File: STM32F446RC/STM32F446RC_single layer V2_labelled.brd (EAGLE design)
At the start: 74.9 x 25.4 mm, 75 parts, among them IC1 STM32F446RCT6

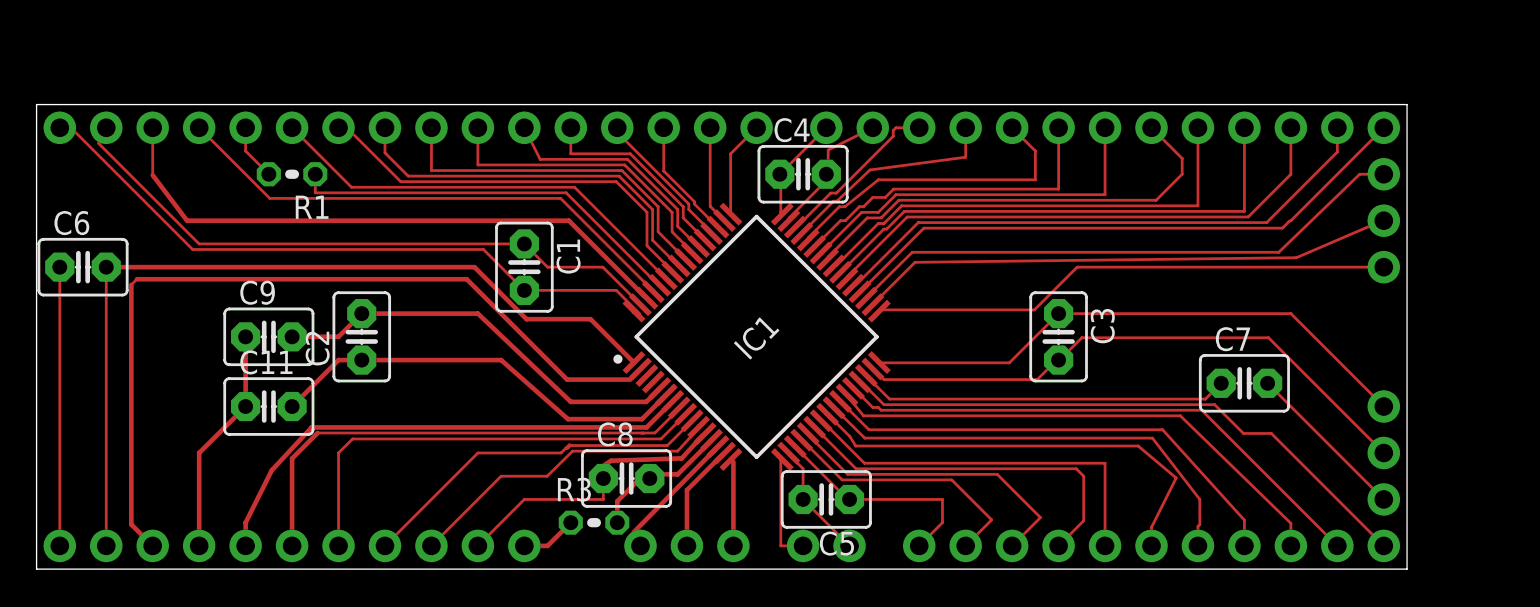
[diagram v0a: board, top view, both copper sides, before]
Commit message: added double layer
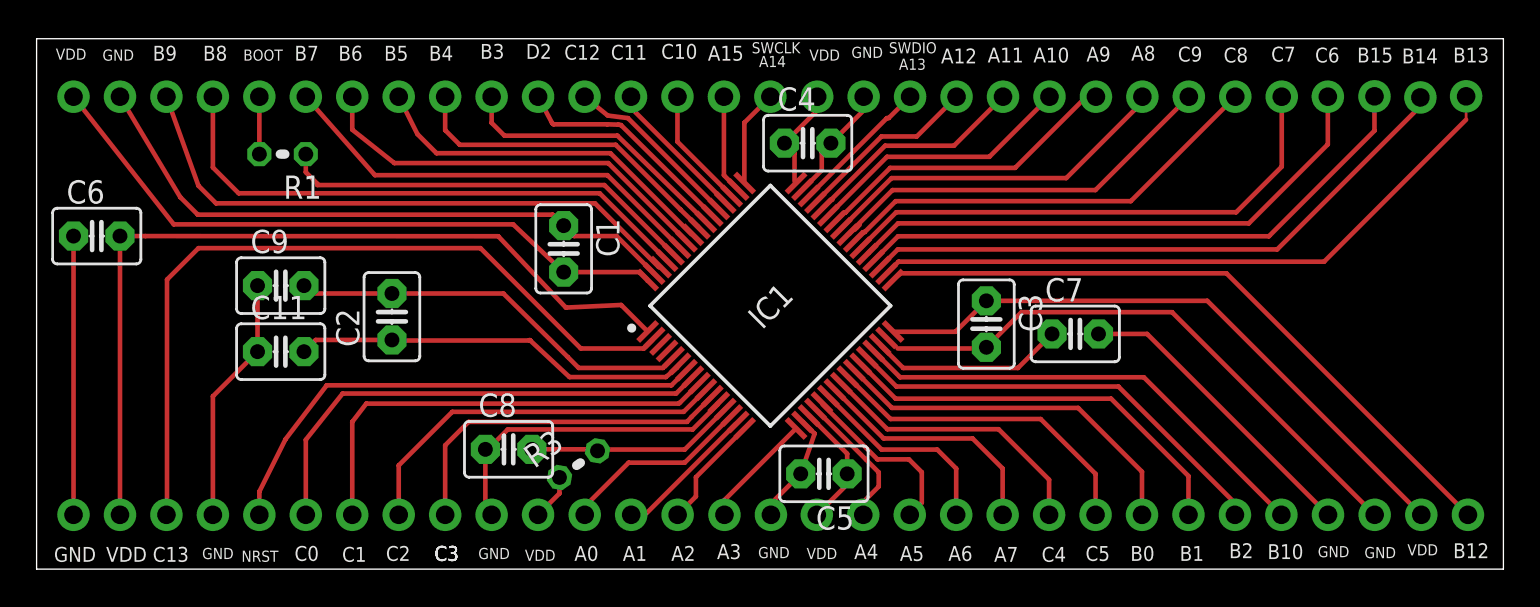
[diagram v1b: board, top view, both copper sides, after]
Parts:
- C1, C3, C4, C5, C6: value 100n+1u -> 100n
- C11, C2, C9: value 20p -> 22p
- R3: value (none) -> 47
- moved JP18 14.3 mm to (78.3, 2.97)
- moved C7 9.64 mm to (56.8, 12.9)
- moved JP13 8.15 mm to (78.2, 25.9)
- moved C8 6.64 mm to (25.8, 6.55)
- moved JP51 6.26 mm to (75.7, 2.97)
- moved JP16 5.85 mm to (65.5, 2.97)
- moved JP22 5.85 mm to (60.4, 2.97)
- moved JP11 5.85 mm to (52.8, 2.97)
- moved JP12 5.85 mm to (55.4, 2.97)
- moved JP17 5.85 mm to (63.0, 2.97)
- moved JP19 5.85 mm to (47.7, 2.97)
- moved JP23 5.85 mm to (57.9, 2.97)
- moved JP48 5.85 mm to (42.7, 2.97)
- moved JP9 5.85 mm to (50.3, 2.97)
- moved JP14 5.85 mm to (68.1, 2.97)
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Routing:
- net N$66: track 20.3 -> 10.7 mm
- net N$11: track 24.5 -> 15.5 mm
- net N$18: track 20.2 -> 11.2 mm
- net N$21: track 28.6 -> 37.0 mm
- net N$54: track 9.09 -> 16.8 mm
- net N$17: track 21.0 -> 13.6 mm
- net N$22: track 29.3 -> 36.7 mm
- net N$19: track 16.8 -> 9.67 mm
- net N$12: track 24.9 -> 18.0 mm
- net N$52: track 14.2 -> 7.65 mm
- net N$16: track 32.3 -> 26.1 mm
- net N$13: track 26.3 -> 20.4 mm
- net N$14: track 28.4 -> 22.7 mm
- net N$15: track 30.0 -> 24.2 mm
- net N$64: track 12.3 -> 7.41 mm
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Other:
- board size 74.9 x 25.4 mm -> 80.2 x 29 mm
- board text added: "A0"
- board text added: "A1"
- board text added: "A10"
- board text added: "A11"
- board text added: "A12"
- board text added: "A13"
- board text added: "A14"
- board text added: "A15"
- board text added: "A2"
- board text added: "A3"
- board text added: "A4"
- board text added: "A5"
- board text added: "A6"
- board text added: "A7"
- board text added: "A8"
- board text added: "A9"
- board text added: "B0"
- board text added: "B1"
- board text added: "B10"
- board text added: "B12"
- board text added: "B13"
- board text added: "B14"
- board text added: "B15"
- board text added: "B2"
- board text added: "B3"
- board text added: "B4"
- board text added: "B5"
- board text added: "B6"
- board text added: "B7"
- board text added: "B8"
- board text added: "B9"
- board text added: "BOOT"
- board text added: "C0"
- board text added: "C1"
- board text added: "C10"
- board text added: "C11"
- board text added: "C12"
- board text added: "C13"
- board text added: "C2"
- board text added: "C3"
- board text added: "C4"
- board text added: "C5"
- board text added: "C6"
- board text added: "C7"
- board text added: "C8"
- board text added: "C9"
- board text added: "D2"
- board text added: "GND"
- board text added: "NRST"
- board text added: "SWCLK"
- board text added: "SWDIO"
- board text added: "VDD"

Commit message: added final
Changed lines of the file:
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@@
 <layer number="16" name="Bottom" color="1" fill="1" visible="yes" active="yes"/>
 <layer number="17" name="Pads" color="2" fill="1" visible="yes" active="yes"/>
-<layer number="18" name="Vias" color="2" fill="1" visible="no" active="yes"/>
+<layer number="18" name="Vias" color="2" fill="1" visible="yes" active="yes"/>
 <layer number="19" name="Unrouted" color="6" fill="1" visible="yes" active="yes"/>
 <layer number="20" name="Dimension" color="24" fill="1" visible="yes" active="yes"/>
 <layer number="21" name="tPlace" color="7" fill="1" visible="yes" active="yes"/>
-<layer number="22" name="bPlace" color="7" fill="1" visible="no" active="yes"/>
+<layer number="22" name="bPlace" color="7" fill="1" visible="yes" active="yes"/>
 <layer number="23" name="tOrigins" color="15" fill="1" visible="yes" active="yes"/>
-<layer number="24" name="bOrigins" color="15" fill="1" visible="no" active="yes"/>
-<layer number="25" name="tNames" color="7" fill="1" visible="no" active="yes"/>
-<layer number="26" name="bNames" color="7" fill="1" visible="no" active="yes"/>
-<layer number="27" name="tValues" color="7" fill="1" visible="no" active="yes"/>
-<layer number="28" name="bValues" color="7" fill="1" visible="no" active="yes"/>
-<layer number="29" name="tStop" color="7" fill="3" visible="no" active="yes"/>
+<layer number="24" name="bOrigins" color="15" fill="1" visible="yes" active="yes"/>
+<layer number="25" name="tNames" color="7" fill="1" visible="yes" active="yes"/>
+<layer number="26" name="bNames" color="7" fill="1" visible="yes" active="yes"/>
+<layer number="27" name="tValues" color="7" fill="1" visible="yes" active="yes"/>
+<layer number="28" name="bValues" color="7" fill="1" visible="yes" active="yes"/>
+<layer number="29" name="tStop" color="7" fill="3" visible="yes" active="yes"/>
 <layer number="30" name="bStop" color="7" fill="6" visible="no" active="yes"/>
-<layer number="31" name="tCream" color="7" fill="4" visible="no" active="yes"/>
-<layer number="32" name="bCream" color="7" fill="5" visible="no" active="yes"/>
-<layer number="33" name="tFinish" color="6" fill="3" visible="no" active="yes"/>
-<layer number="34" name="bFinish" color="6" fill="6" visible="no" active="yes"/>
-<layer number="35" name="tGlue" color="7" fill="4" visible="no" active="yes"/>
-<layer number="36" name="bGlue" color="7" fill="5" visible="no" active="yes"/>
-<layer number="37" name="tTest" color="7" fill="1" visible="no" active="yes"/>
-<layer number="38" name="bTest" color="7" fill="1" visible="no" active="yes"/>
-<layer number="39" name="tKeepout" color="4" fill="11" visible="no" active="yes"/>
-<layer number="40" name="bKeepout" color="1" fill="11" visible="no" active="yes"/>
-<layer number="41" name="tRestrict" color="4" fill="10" visible="no" active="yes"/>
-<layer number="42" name="bRestrict" color="1" fill="10" visible="no" active="yes"/>
-<layer number="43" name="vRestrict" color="2" fill="10" visible="no" active="yes"/>
-<layer number="44" name="Drills" color="7" fill="1" visible="no" active="yes"/>
-<layer number="45" name="Holes" color="7" fill="1" visible="no" active="yes"/>
-<layer number="46" name="Milling" color="3" fill="1" visible="no" active="yes"/>
-<layer number="47" name="Measures" color="7" fill="1" visible="no" active="yes"/>
+<layer number="31" name="tCream" color="7" fill="4" visible="yes" active="yes"/>
+<layer number="32" name="bCream" color="7" fill="5" visible="yes" active="yes"/>
+<layer number="33" name="tFinish" color="6" fill="3" visible="yes" active="yes"/>
+<layer number="34" name="bFinish" color="6" fill="6" visible="yes" active="yes"/>
+<layer number="35" name="tGlue" color="7" fill="4" visible="yes" active="yes"/>
+<layer number="36" name="bGlue" color="7" fill="5" visible="yes" active="yes"/>
+<layer number="37" name="tTest" color="7" fill="1" visible="yes" active="yes"/>
+<layer number="38" name="bTest" color="7" fill="1" visible="yes" active="yes"/>
+<layer number="39" name="tKeepout" color="4" fill="11" visible="yes" active="yes"/>
+<layer number="40" name="bKeepout" color="1" fill="11" visible="yes" active="yes"/>
+<layer number="41" name="tRestrict" color="4" fill="10" visible="yes" active="yes"/>
+<layer number="42" name="bRestrict" color="1" fill="10" visible="yes" active="yes"/>
+<layer number="43" name="vRestrict" color="2" fill="10" visible="yes" active="yes"/>
+<layer number="44" name="Drills" color="7" fill="1" visible="yes" active="yes"/>
+<layer number="45" name="Holes" color="7" fill="1" visible="yes" active="yes"/>
+<layer number="46" name="Milling" color="3" fill="1" visible="yes" active="yes"/>
+<layer number="47" name="Measures" color="7" fill="1" visible="yes" active="yes"/>
 <layer number="48" name="Document" color="7" fill="1" visible="yes" active="yes"/>
-<layer number="49" name="Reference" color="7" fill="1" visible="no" active="yes"/>
+<layer number="49" name="Reference" color="7" fill="1" visible="yes" active="yes"/>
 <layer number="50" name="dxf" color="7" fill="1" visible="no" active="no"/>
-<layer number="51" name="tDocu" color="7" fill="1" visible="no" active="yes"/>
+<layer number="51" name="tDocu" color="7" fill="1" visible="yes" active="yes"/>
 <layer number="52" name="bDocu" color="7" fill="1" visible="yes" active="yes"/>
 <layer number="53" name="tGND_GNDA" color="7" fill="1" visible="no" active="no"/>
@@
 <layer number="221" name="221bmp" color="7" fill="1" visible="yes" active="yes"/>
 <layer number="222" name="222bmp" color="7" fill="1" visible="yes" active="yes"/>
-<layer number="223" name="223bmp" color="7" fill="1" visible="no" active="yes"/>
-<layer number="224" name="224bmp" color="7" fill="1" visible="no" active="yes"/>
-<layer number="250" name="Descript" color="7" fill="1" visible="no" active="yes"/>
-<layer number="251" name="SMDround" color="7" fill="1" visible="no" active="yes"/>
-<layer number="254" name="cooling" color="7" fill="1" visible="no" active="yes"/>
+<layer number="223" name="223bmp" color="7" fill="1" visible="yes" active="yes"/>
+<layer number="224" name="224bmp" color="7" fill="1" visible="yes" active="yes"/>
+<layer number="250" name="Descript" color="7" fill="1" visible="yes" active="yes"/>
+<layer number="251" name="SMDround" color="7" fill="1" visible="yes" active="yes"/>
+<layer number="254" name="cooling" color="7" fill="1" visible="yes" active="yes"/>
 </layers>
 <board>
@@
 <contactref element="IC1" pad="1"/>
 <wire x1="33.41096875" y1="12.99426875" x2="33.3636" y2="13.13" width="0.1524" layer="1"/>
-<wire x1="33.41096875" y1="12.99426875" x2="31.962575" y2="14.4426625" width="0.254" layer="1"/>
+<wire x1="33.41096875" y1="12.99426875" x2="31.876096875" y2="14.529140625" width="0.254" layer="1"/>
 <wire x1="5.950053125" y1="18.209309375" x2="4.56" y2="18.21" width="0.254" layer="1"/>
 <wire x1="25.2420125" y1="18.199728125" x2="5.950053125" y2="18.209309375" width="0.254" layer="1"/>
-<wire x1="28.93999375" y1="14.3" x2="25.2420125" y2="18.199728125" width="0.254" layer="1"/>
-<wire x1="31.962575" y1="14.4426625" x2="28.93999375" y2="14.3" width="0.254" layer="1"/>
+<wire x1="28.857796875" y1="14.38668125" x2="25.2420125" y2="18.199728125" width="0.254" layer="1"/>
+<wire x1="31.876096875" y1="14.529140625" x2="28.857796875" y2="14.38668125" width="0.254" layer="1"/>
 <wire x1="4.56" y1="18.21" x2="4.56" y2="2.97" width="0.254" layer="1"/>
 </signal>
